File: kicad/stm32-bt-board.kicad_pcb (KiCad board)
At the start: 4 copper layers, 48 x 33 mm, 60 parts

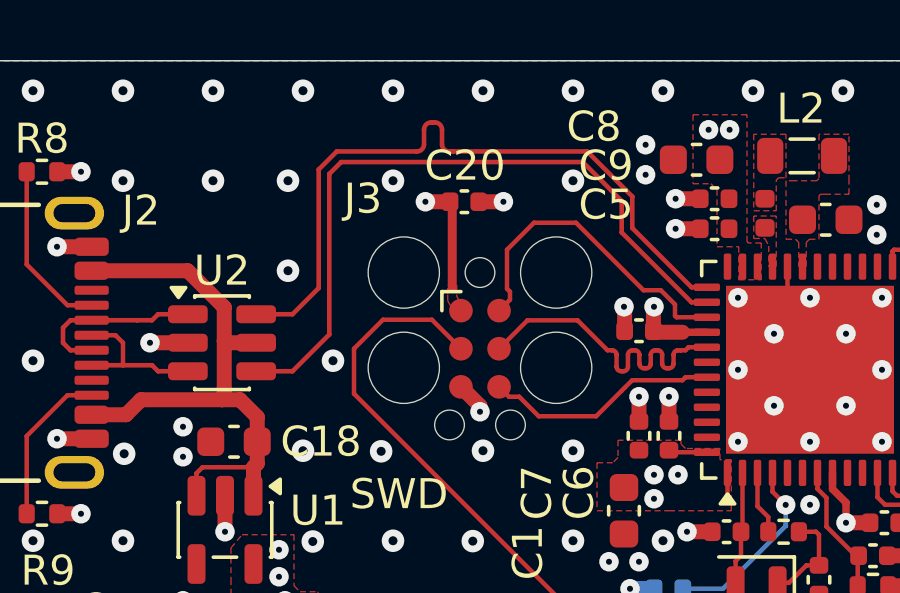
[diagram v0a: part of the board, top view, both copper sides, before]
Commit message: feat(layout & manuf.): add USB clearance and regenerate manufacturing files
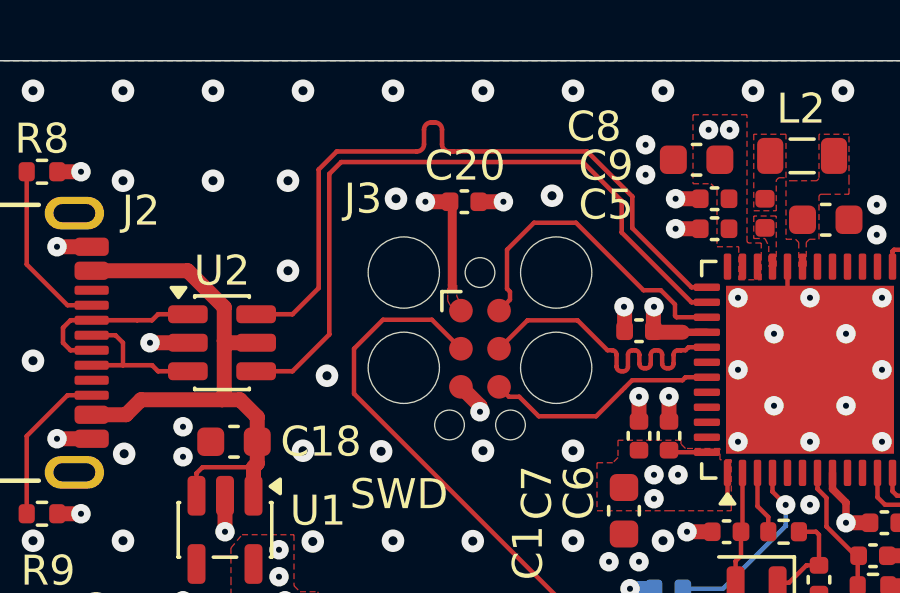
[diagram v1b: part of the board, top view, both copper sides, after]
